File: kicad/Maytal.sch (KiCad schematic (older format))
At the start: 6 parts, among them IC1 ArduinoProMini, P1 LIPO_SOLAR, P2 CONN_01X03, Q1 PN2222A, U1 FONA_808, U2 Adafruit_DS3231

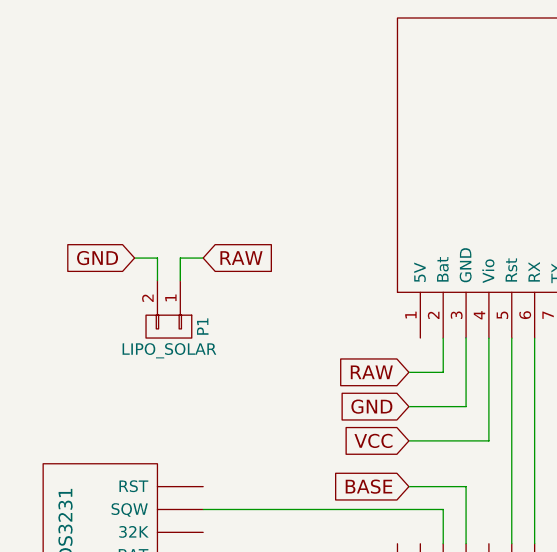
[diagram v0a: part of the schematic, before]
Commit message: Rerouted power bus
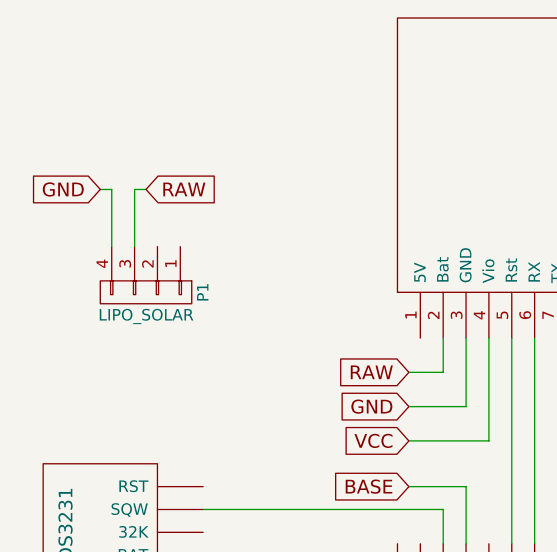
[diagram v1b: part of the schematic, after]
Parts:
- removed P1: LIPO_SOLAR, DAI_Maker_Lab_footprints:Adafruit_LiPo_Solar, symbol CONN_01X02
- added P1: LIPO_SOLAR, DAI_Maker_Lab_footprints:Adafruit_LiPo_Solar, symbol CONN_01X04
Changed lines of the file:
@@
 Text GLabel 4050 4400 2    60   Input ~ 0
 SCL
-$Comp
-L CONN_01X02 P1
-U 1 1 58C05A2A
-P 3600 3200
-F 0 "P1" H 3600 3350 50  0000 C CNN
-F 1 "LIPO_SOLAR" V 3700 3200 50  0000 C CNN
-F 2 "DAI_Maker_Lab_footprints:Adafruit_LiPo_Solar" H 3600 3200 50  0001 C CNN
-F 3 "" H 3600 3200 50  0000 C CNN
-	1    3600 3200
-	0    1    1    0
-$EndComp
-Text GLabel 3750 2900 2    60   Input ~ 0
+Text GLabel 3500 2600 2    60   Input ~ 0
 RAW
-Text GLabel 3450 2900 0    60   Input ~ 0
+Text GLabel 3300 2600 0    60   Input ~ 0
 GND
 $Comp
@@
 Wire Wire Line
 	3800 4300 3750 4300
-Wire Wire Line
-	3450 2900 3550 2900
-Wire Wire Line
-	3550 2900 3550 3000
-Wire Wire Line
-	3750 2900 3650 2900
-Wire Wire Line
-	3650 2900 3650 3000
 Wire Wire Line
 	6700 6050 6700 6150
@@
 Wire Wire Line
 	5500 3750 5500 4150
+$Comp
+L CONN_01X04 P1
+U 1 1 59552F28
+P 3500 3050
+F 0 "P1" H 3500 3300 50  0000 C CNN
+F 1 "LIPO_SOLAR" V 3600 3050 50  0000 C CNN
+F 2 "DAI_Maker_Lab_footprints:Adafruit_LiPo_Solar" H 3500 3050 50  0001 C CNN
+F 3 "" H 3500 3050 50  0000 C CNN
+	1    3500 3050
+	0    1    1    0
+$EndComp
+Wire Wire Line
+	3300 2600 3350 2600
+Wire Wire Line
+	3350 2600 3350 2850
+Wire Wire Line
+	3500 2600 3450 2600
+Wire Wire Line
+	3450 2600 3450 2850
 $EndSCHEMATC
